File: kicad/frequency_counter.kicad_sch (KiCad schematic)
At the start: 23 parts, among them J101 CH.A, J102 J, J103 DISPLAY, SW101 SPDT, SW102 PEC12R

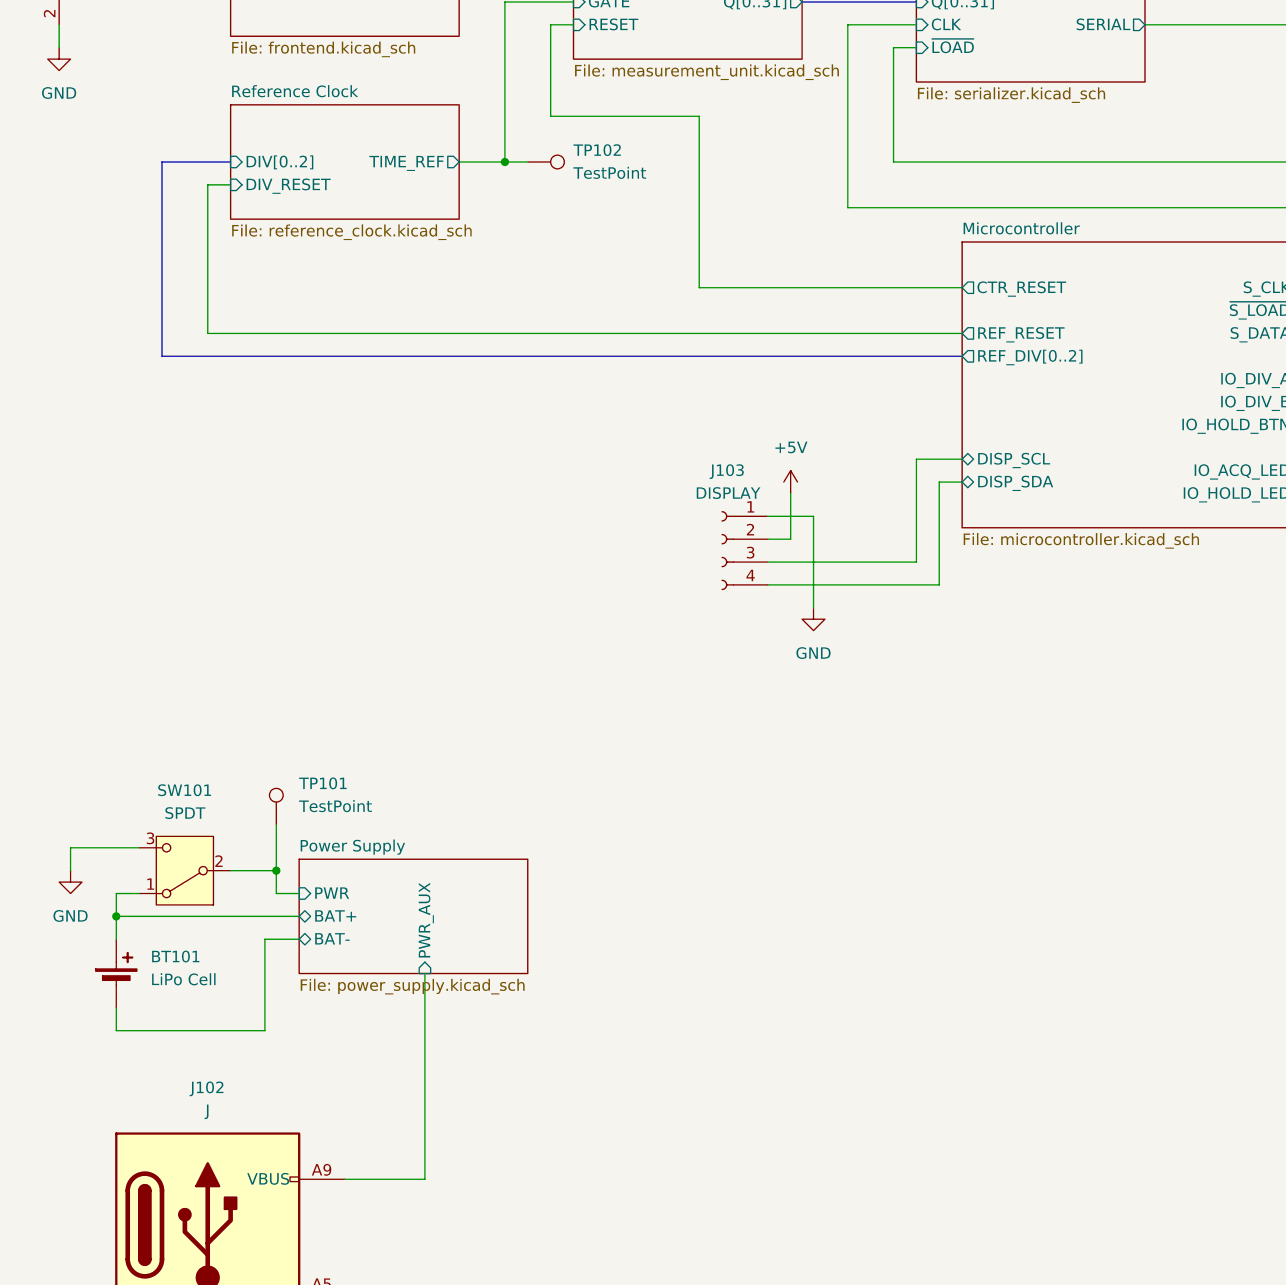
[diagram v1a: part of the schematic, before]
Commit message: add i2c pullups, fix power switch + tp, update block
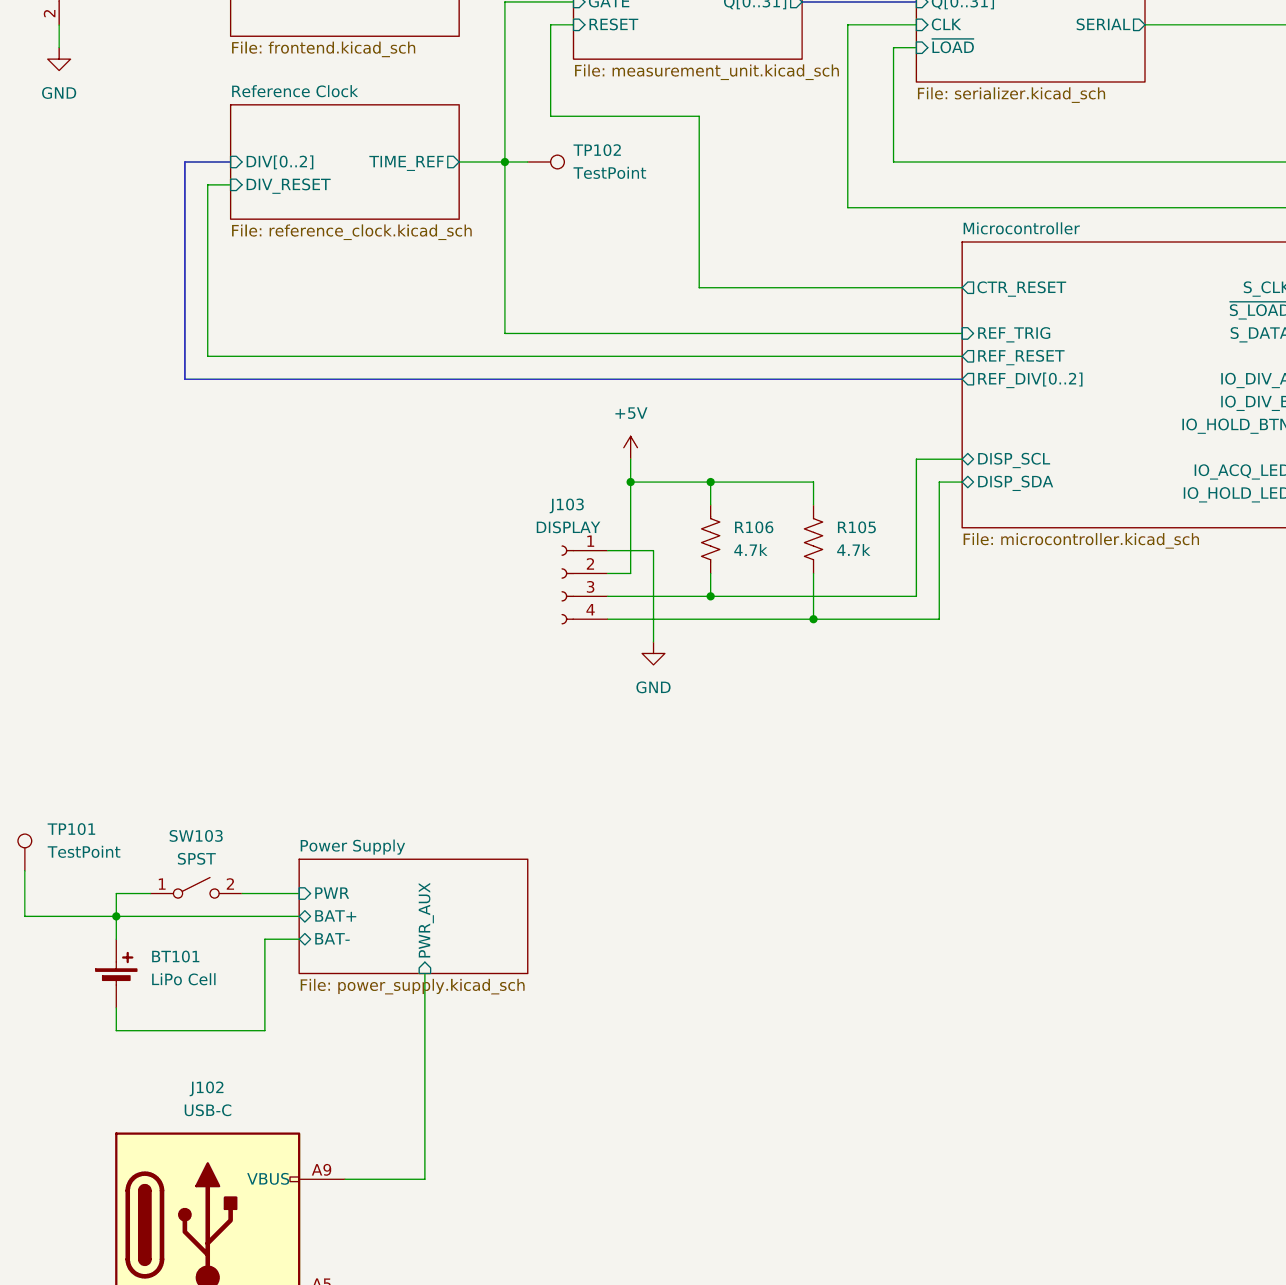
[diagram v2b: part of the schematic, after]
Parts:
- removed SW101: SPDT, Connector_Wire:SolderWire-0.5sqmm_1x03_P4.6mm_D0.9mm_OD2.1mm, symbol Switch:SW_SPDT
- added R105, R106: 4.7k, symbol Device:R_US
- added SW103: SPST, Connector_Wire:SolderWire-1.5sqmm_1x02_P6mm_D1.7mm_OD3mm, symbol Switch:SW_SPST
- J102: value J -> USB-C
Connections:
- net +5V: now also R105.1, R106.1
- net Microcontroller/DISP_SCL: now also R106.2
- net Microcontroller/DISP_SDA: now also R105.2
- net Power Supply/BAT+: now also TP101.1, SW103.1 (A)
- net Power Supply/PWR: now also SW103.2 (B); no longer TP101.1
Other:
- sheet Microcontroller ports: added REF_TRIG; removed none
- moved on the sheet: J103, TP101

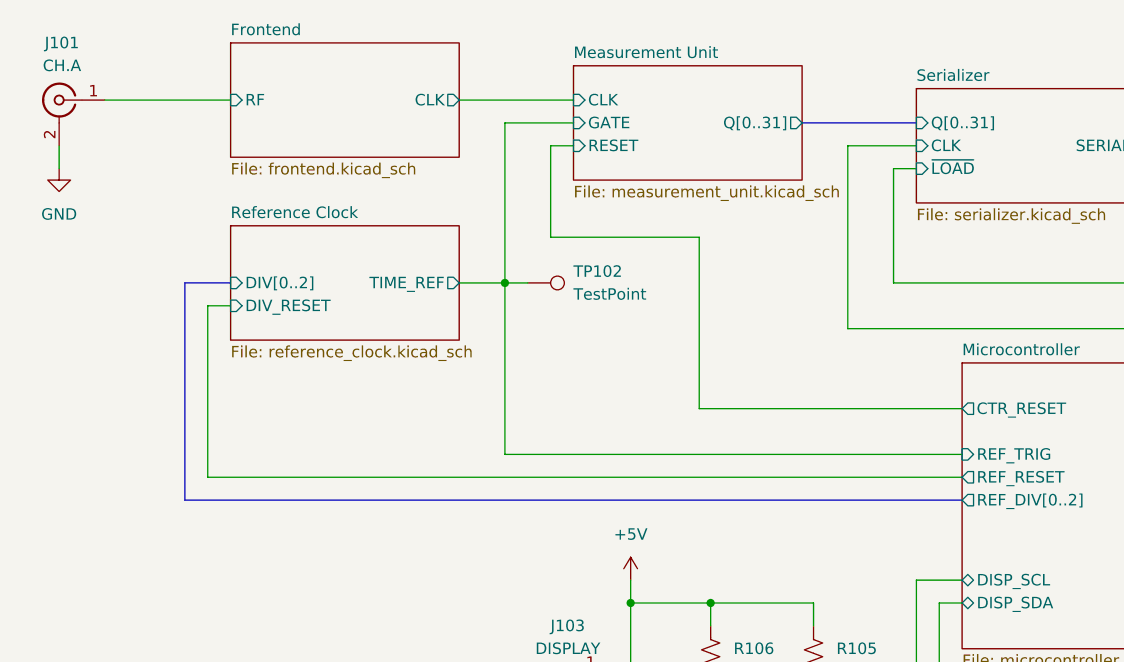
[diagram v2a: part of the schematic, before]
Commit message: split frontend into two channels
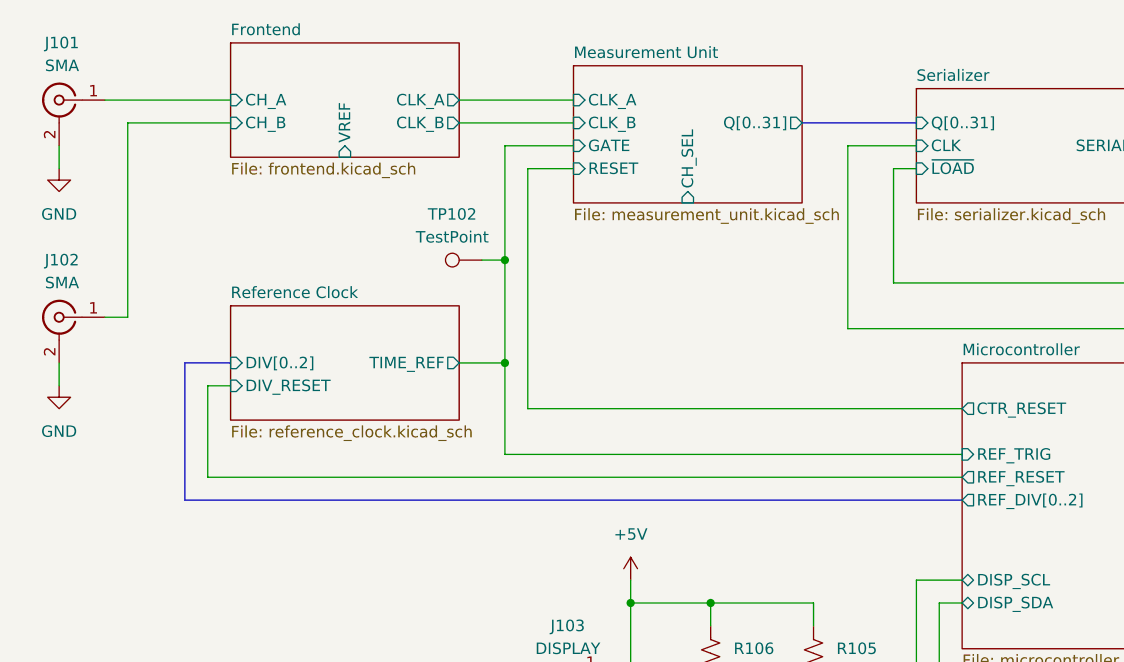
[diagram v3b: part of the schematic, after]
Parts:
- added J102: SMA, Custom:SMA_Adjusted, symbol Connector:Conn_Coaxial
- J101: value CH.A -> SMA
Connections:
- net GND: now also J102.2 (Ext)
- net Frontend/RF renamed Frontend/CH_A
- new net Frontend/CH_B: J102.1 (In)
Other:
- sheet Frontend ports: added CH_A, CH_B, CLK_A, CLK_B, VREF; removed CLK, RF
- sheet Measurement Unit ports: added CH_SEL, CLK_A, CLK_B; removed CLK
- moved on the sheet: TP102

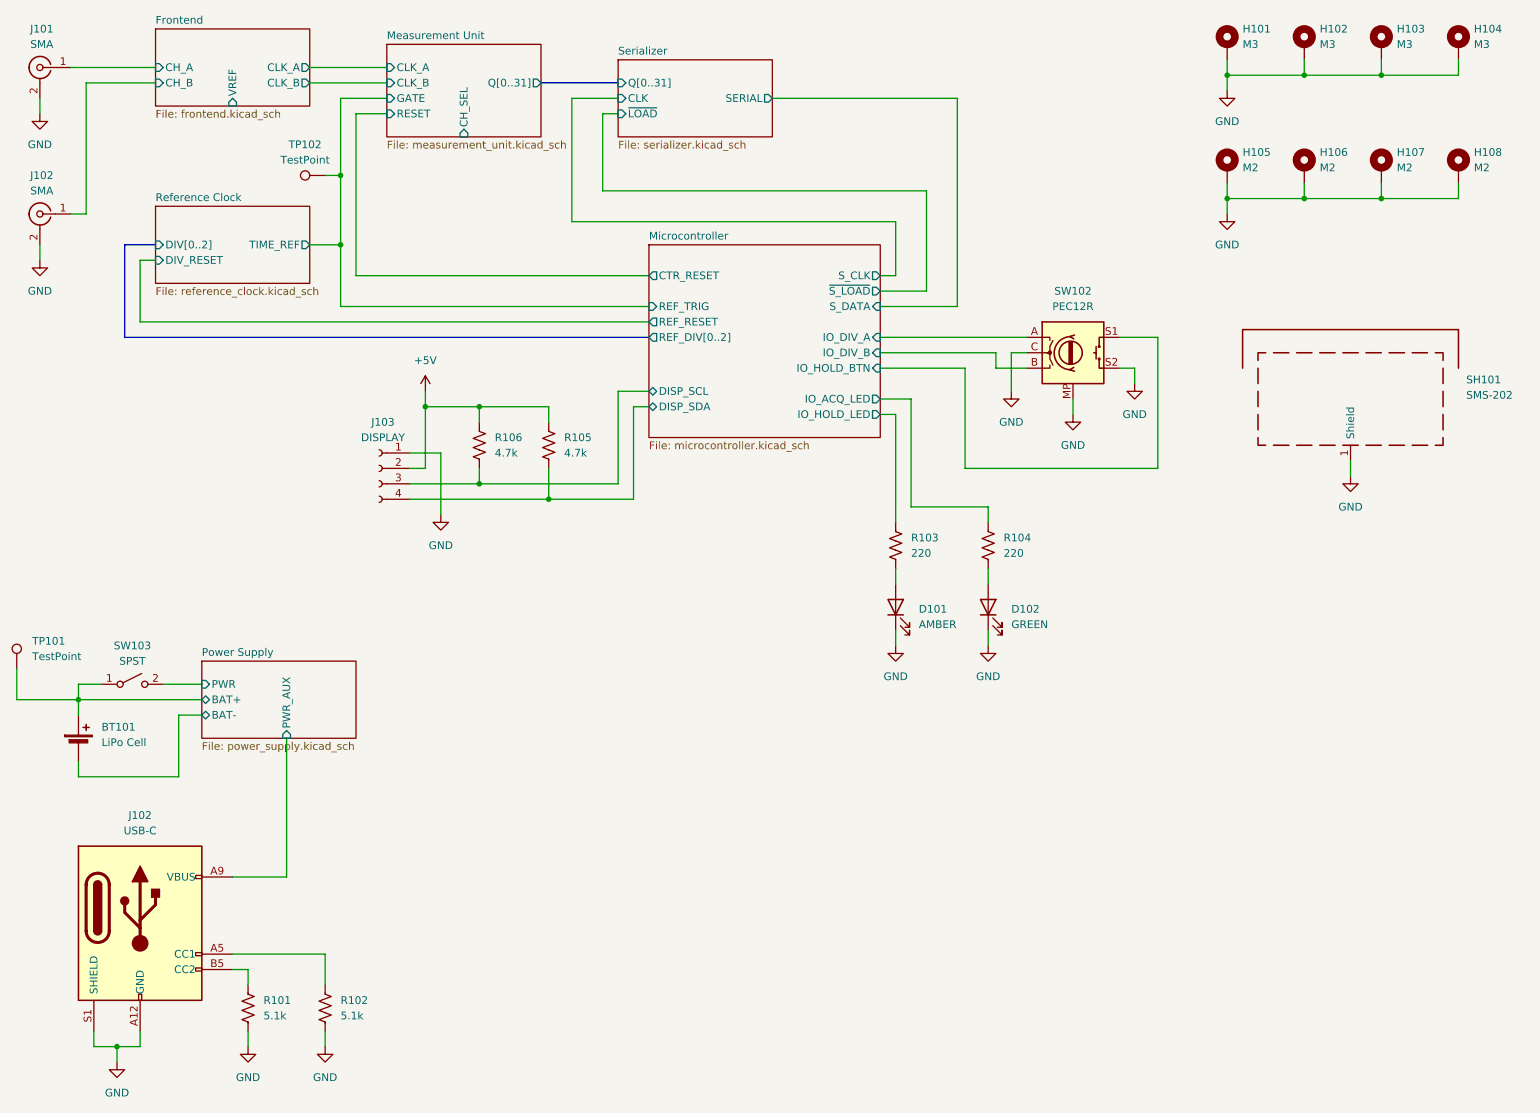
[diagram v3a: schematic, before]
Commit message: swap encoder for two buttons, assign channel select pin
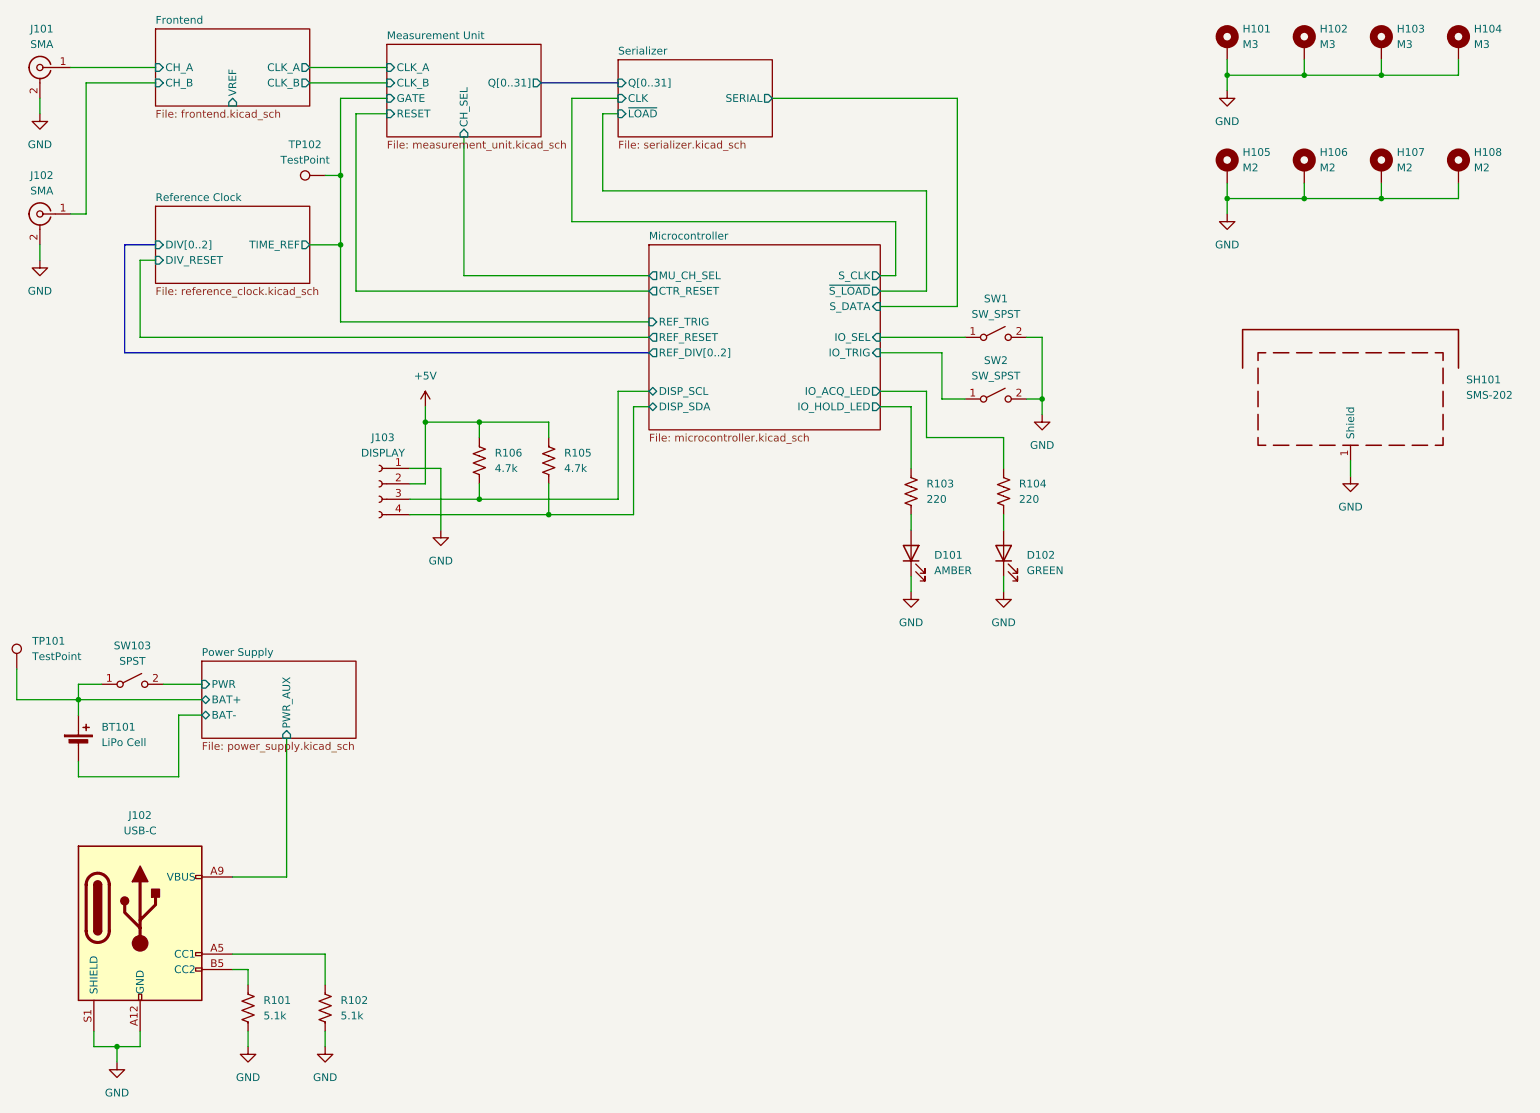
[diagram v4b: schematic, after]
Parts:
- removed SW102: PEC12R, Rotary_Encoder:RotaryEncoder_Alps_EC11E-Switch_Vertical_H20mm, symbol Custom:PEC12R
- added SW1, SW2: SW_SPST, symbol Switch:SW_SPST
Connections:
- net GND: now also SW1.2 (B), SW2.2 (B)
- new net Microcontroller/IO_SEL: SW1.1 (A)
- new net Microcontroller/IO_TRIG: SW2.1 (A)
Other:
- sheet Microcontroller ports: added IO_SEL, IO_TRIG, MU_CH_SEL; removed IO_DIV_A, IO_DIV_B, IO_HOLD_BTN
- moved on the sheet: D101, D102, J103, R103, R104, R105, R106
